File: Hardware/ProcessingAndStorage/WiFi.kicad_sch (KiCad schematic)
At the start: 14 parts, among them J5 Conn_02x11_Odd_Even, SW2 SW_SPDT_XKB_DMx-xxxx-1, U2 ESP-12E

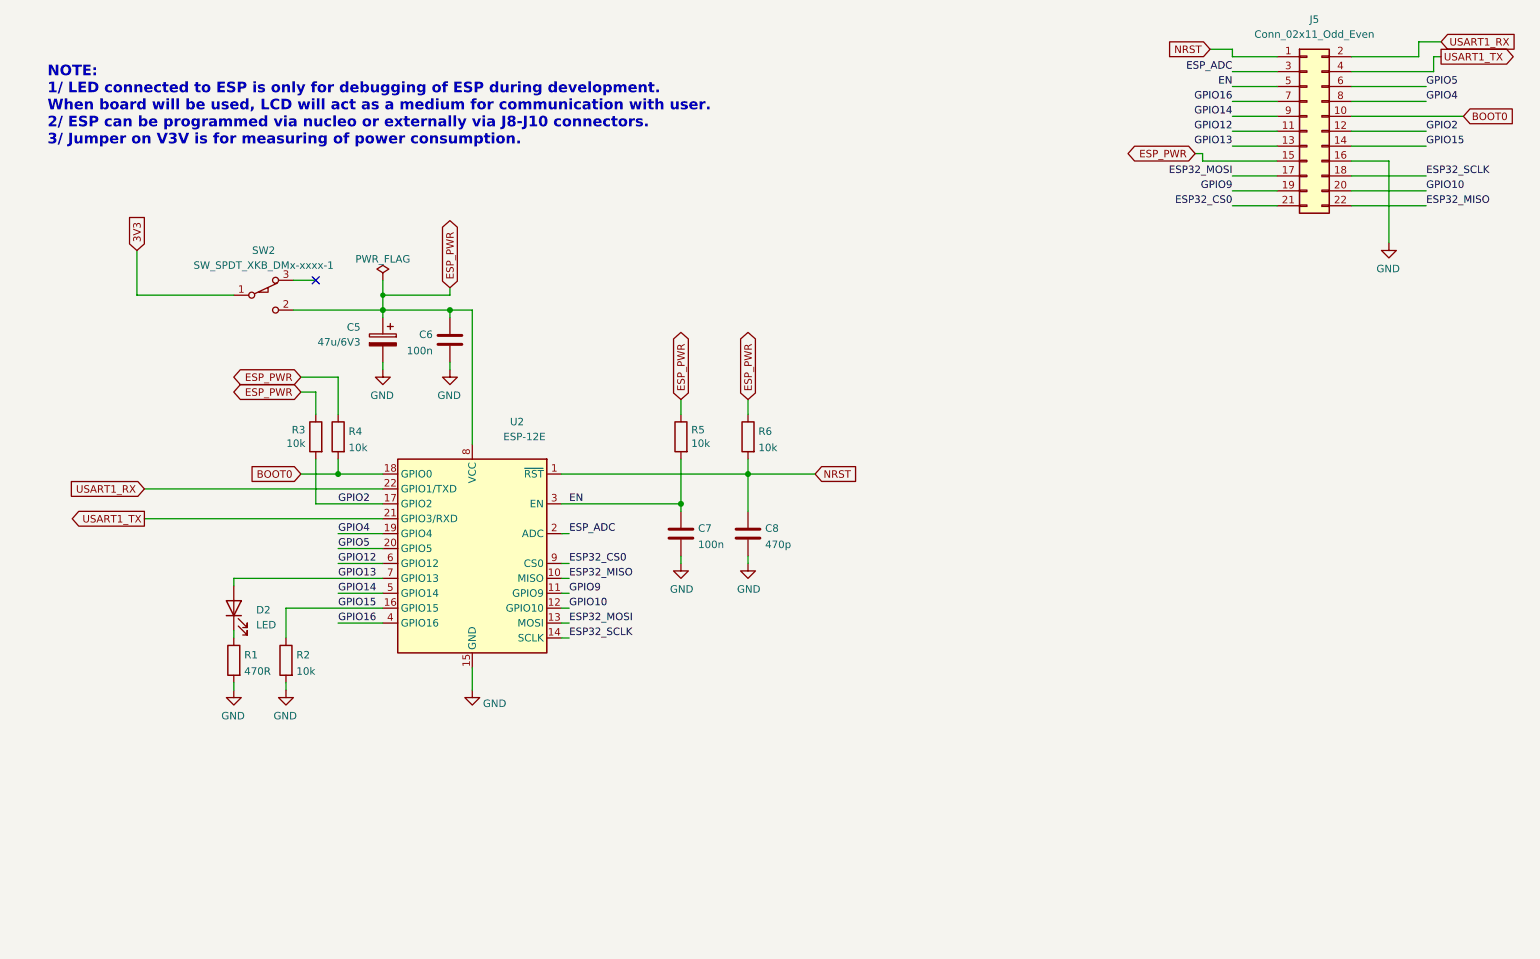
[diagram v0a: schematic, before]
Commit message: rework CI, make PCB smaller
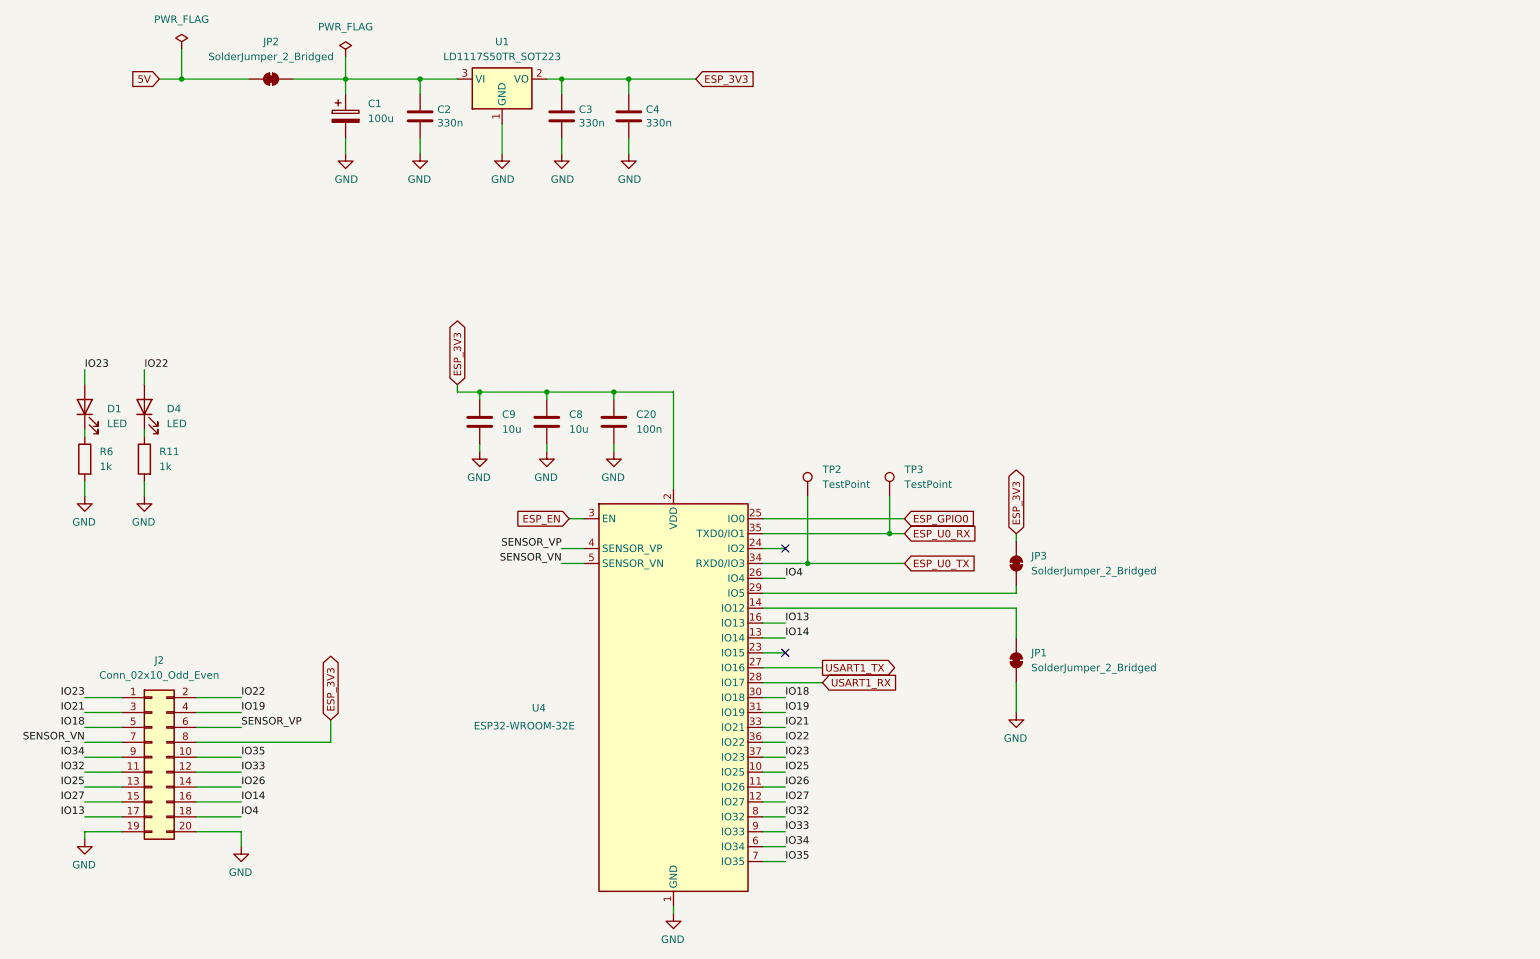
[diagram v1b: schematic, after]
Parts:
- removed C5: 47u/6V3, Capacitor_Tantalum_SMD:CP_EIA-3528-21_Kemet-B, symbol Device:C_Polarized
- removed C6, C7: 100n, Capacitor_SMD:C_0805_2012Metric, symbol Device:C
- removed D2: LED, LED_SMD:LED_0402_1005Metric, symbol Device:LED
- removed J5: Conn_02x11_Odd_Even, Connector_PinHeader_2.54mm:PinHeader_2x11_P2.54mm_Vertical, symbol Connector_Generic:Conn_02x11_Odd_Even
- removed R1: 470R, Resistor_SMD:R_0805_2012Metric, symbol Device:R
- removed R2, R3, R4, R5: 10k, Resistor_SMD:R_0805_2012Metric, symbol Device:R
- removed SW2: SW_SPDT_XKB_DMx-xxxx-1, Button_Switch_THT:SW_Slide-03_Wuerth-WS-SLTV_10x2.5x6.4_P2.54mm, symbol Switch:SW_SPDT_XKB_DMx-xxxx-1
- removed U2: ESP-12E, RF_Module:ESP-12E, symbol RF_Module:ESP-12E
- added C1: 100u, Capacitor_SMD:CP_Elec_6.3x5.8, symbol Device:C_Polarized
- added C2, C3, C4: 330n, Capacitor_SMD:C_0805_2012Metric, symbol Device:C
- added C20: 100n, Capacitor_SMD:C_0805_2012Metric, symbol Device:C
- added C9: 10u, Capacitor_SMD:C_0805_2012Metric, symbol Device:C
- added D1, D4: LED, LED_SMD:LED_0402_1005Metric, symbol Device:LED
- added J2: Conn_02x10_Odd_Even, Connector_PinHeader_2.54mm:PinHeader_2x10_P2.54mm_Horizontal, symbol Connector_Generic:Conn_02x10_Odd_Even
- added JP1, JP2, JP3: SolderJumper_2_Bridged, Jumper:SolderJumper-2_P1.3mm_Bridged_Pad1.0x1.5mm, symbol Jumper:SolderJumper_2_Bridged
- added R11: 1k, Resistor_SMD:R_0805_2012Metric, symbol Device:R
- added TP2, TP3: TestPoint, TestPoint:TestPoint_Pad_D1.5mm, symbol Connector:TestPoint
- added U1: LD1117S50TR_SOT223, Package_TO_SOT_SMD:SOT-223-3_TabPin2, symbol Regulator_Linear:LD1117S50TR_SOT223
- added U4: ESP32-WROOM-32E, RF_Module:ESP32-WROOM-32D, symbol RF_Module:ESP32-WROOM-32E
- C8: value 470p -> 10u
- R6: value 10k -> 1k
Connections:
- net GND: now also R6.2, C1.2, C2.2, C20.2, C3.2, C4.2, C9.2, J2.19 (Pin_19), J2.20 (Pin_20), JP1.1 (A), R11.2, U1.1 (GND), U4.1 (GND), U4.15 (GND), U4.38 (GND), U4.39 (GND)
- net USART1_RX: now also U4.28 (IO17)
- net USART1_TX: now also U4.27 (IO16)
- net ESP_PWR: no longer names the net of R6.1
- net ESP_PWR: now also D1.1 (K)
- net NRST renamed ESP_3V3
- net ESP_3V3: now also C20.1, C3.1, C4.1, C9.1, J2.8 (Pin_8), JP3.2 (B), U1.2 (VO), U4.2 (VDD); no longer R6.2
- new net: JP3.1 (A), U4.29 (IO5)
- new net: C1.1, C2.1, JP2.2 (B), U1.3 (VI)
- new net: JP1.2 (B), U4.14 (IO12)
- new net: D4.1 (K), R11.1
- new net 5V: JP2.1 (A)
- new net ESP_EN: U4.3 (EN)
- new net ESP_GPIO0: U4.25 (IO0)
- new net ESP_U0_RX: TP3.1, U4.35 (TXD0/IO1)
- new net ESP_U0_TX: TP2.1, U4.34 (RXD0/IO3)
- new net IO13: J2.17 (Pin_17), U4.16 (IO13)
- new net IO14: J2.16 (Pin_16), U4.13 (IO14)
- new net IO18: J2.5 (Pin_5), U4.30 (IO18)
- new net IO19: J2.4 (Pin_4), U4.31 (IO19)
- new net IO21: J2.3 (Pin_3), U4.33 (IO21)
- new net IO22: D4.2 (A), J2.2 (Pin_2), U4.36 (IO22)
- new net IO23: D1.2 (A), J2.1 (Pin_1), U4.37 (IO23)
- new net IO25: J2.13 (Pin_13), U4.10 (IO25)
- new net IO26: J2.14 (Pin_14), U4.11 (IO26)
- new net IO27: J2.15 (Pin_15), U4.12 (IO27)
- new net IO32: J2.11 (Pin_11), U4.8 (IO32)
- new net IO33: J2.12 (Pin_12), U4.9 (IO33)
- new net IO34: J2.9 (Pin_9), U4.6 (IO34)
- new net IO35: J2.10 (Pin_10), U4.7 (IO35)
- new net IO4: J2.18 (Pin_18), U4.26 (IO4)
- new net SENSOR_VN: J2.7 (Pin_7), U4.5 (SENSOR_VN)
- new net SENSOR_VP: J2.6 (Pin_6), U4.4 (SENSOR_VP)
- no-connect marks 1 -> 2
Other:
- note removed: "NOTE: 1/ LED connected to ESP is only for debugging of ESP during development. When board will be used, LCD will act as a medium for communication with user. 2/ ESP can be programmed via nucleo or externally via J8-J10 connectors. 3/ Jumper on V3V is for measuring of power consumption."
